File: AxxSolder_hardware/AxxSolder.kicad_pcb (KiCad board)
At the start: 2 copper layers, 39 x 82.5 mm, 143 parts, among them IC1 TLV76733DRVR, IC2 OPA2387DSGT, IC3 LMR54406DBVR, IC4 STM32G431CBT6, IC5 TPD4E1U06DBVR, IC6 STUSB4500QTR, IC7 MAX16171ATA_VY+T, IC8 LTC4440AHMS8E, IC9 INA281A5QDBVRQ1, J1 USB4110-GF-A, J2 691243110009, J3 TSW-102-07-T-S, J4 61300611821, J5 TSW-102-07-T-S, J6 TSW-102-07-T-S, Q1 STL9P3LLH6, Q2 STL10N3LLH5, Q3 2N7002NXAKR, U2 PEC11J-9215F-S0015, U3 BSC014N04LS

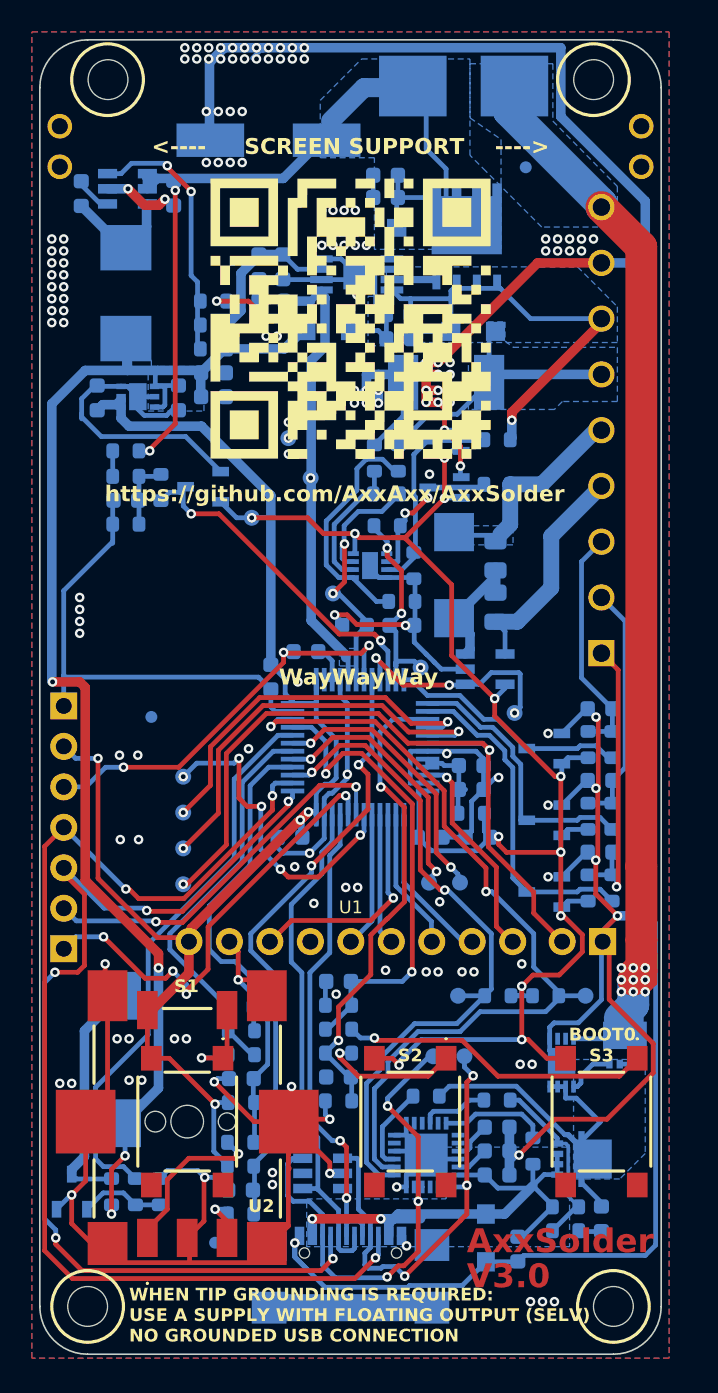
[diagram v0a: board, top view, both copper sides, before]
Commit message: Update hardware files to match correctly with current version
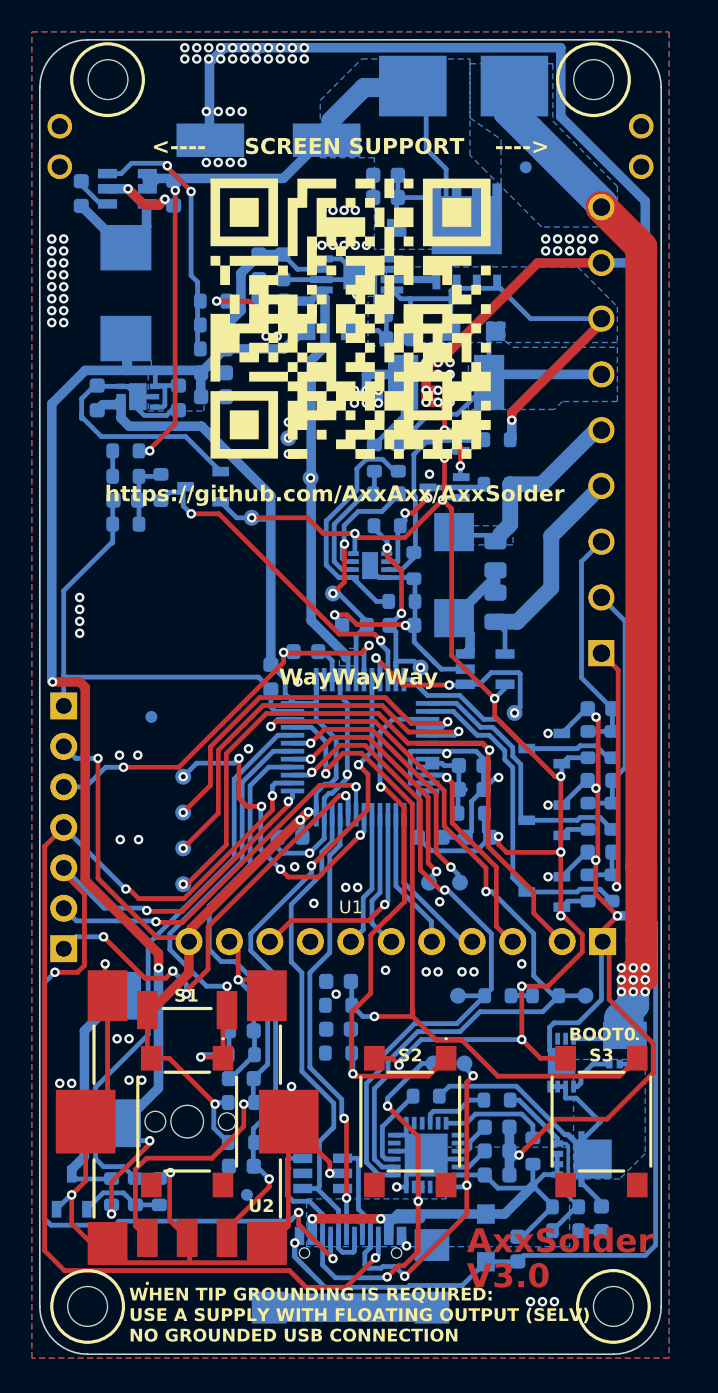
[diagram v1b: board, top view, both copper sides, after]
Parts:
- removed R16, R43, R46, R47, R48: 100, Resistor_SMD:R_0603_1608Metric
- moved FID2 3.61 mm to (174.0, 140.0)
- moved C22 3.00 mm to (179.8, 129.6)
- moved R31 3.00 mm to (179.8, 131.1)
- moved C29 1.50 mm to (173.7, 138.2)
- moved C21 1.50 mm to (173.7, 129.7)
- moved R30 1.50 mm to (173.7, 131.2)
- moved R36 1.49 mm to (173.7, 136.7)
- moved TP7 0.45 mm to (187.7, 131.8)
- moved TP8 0.45 mm to (185.7, 131.8)
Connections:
- J1 pad S1: (no net) -> unconnected-(J1-SHIELD-PadS1)
- S1 pad 1: /S1 -> /SW1
- S2 pad 1: Net-(R43-Pad2) -> /SW2
- S3 pad 1: Net-(R46-Pad2) -> /SW3
- U2 pad A1: Net-(R47-Pad2) -> /ENC_B
- U2 pad C1: Net-(R48-Pad2) -> /ENC_A
- U2 pad E1: /S1 -> /SW1
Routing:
- net Net-(R46-Pad2): track 19.7 -> 0.00 mm, vias 1 -> 0
- net /SW3: track 30.4 -> 47.3 mm
- net GND: track 460.3 -> 447.9 mm, vias 157 -> 149
- net /ENC_B: track 29.0 -> 41.0 mm, vias 0 -> 1
- net Net-(R47-Pad2): track 10.3 -> 0.00 mm, vias 1 -> 0
- net (no net): track 10.2 -> 0.00 mm
- net unconnected-(J1-SHIELD-PadS1): track 0.00 -> 10.2 mm
- net Net-(R43-Pad2): track 9.08 -> 0.00 mm, vias 1 -> 0
- net /SW2: track 30.1 -> 36.6 mm
- net /S1: track 6.25 -> 0.00 mm, vias 1 -> 0
- net /SW1: track 25.3 -> 30.3 mm, vias 0 -> 2
- net /ENC_A: track 38.3 -> 41.5 mm, vias 2 -> 3
- net Net-(R48-Pad2): track 2.95 -> 0.00 mm, vias 1 -> 0
- net +7.5V: track 94.1 -> 95.8 mm
- net /USB_D+: track 32.5 -> 33.4 mm

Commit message: Update hw design with button filters, optimized traces and better silkscreen
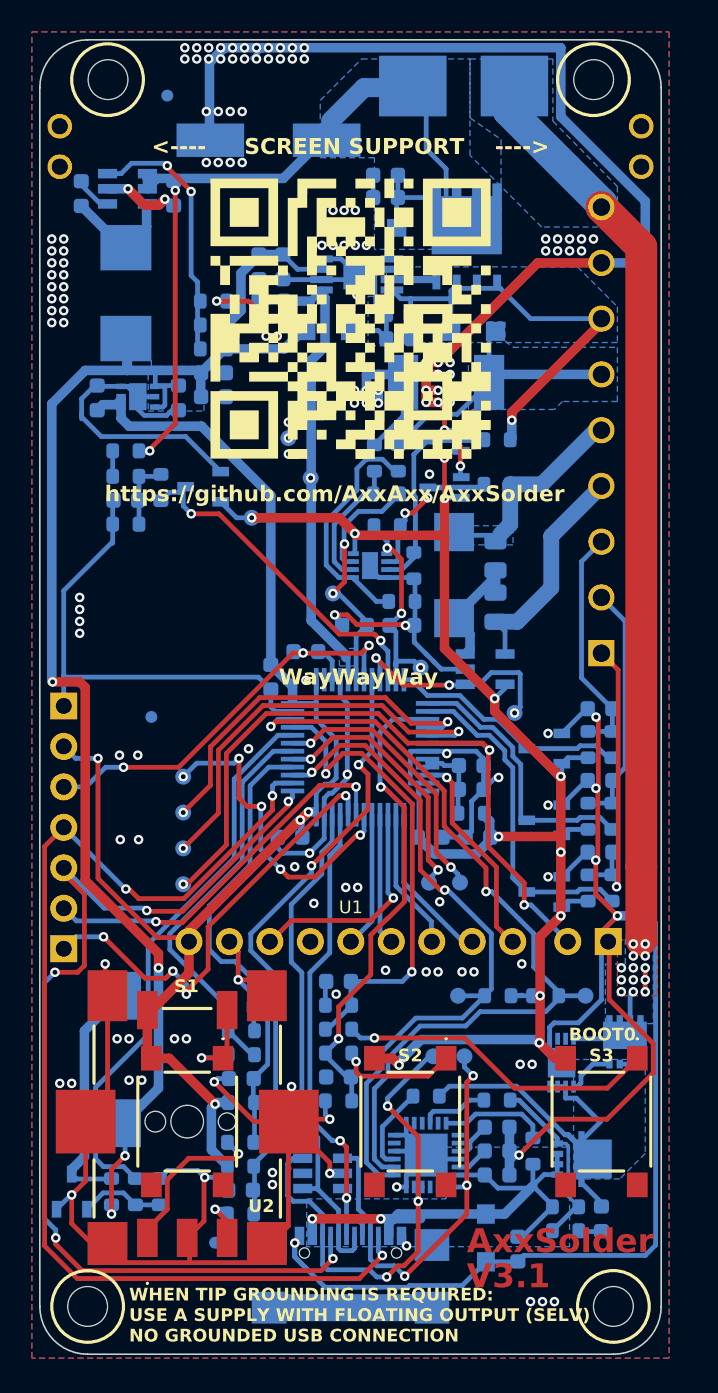
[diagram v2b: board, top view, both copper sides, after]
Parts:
- added R16: 100, Resistor_SMD:R_0603_1608Metric, B.Cu at (173.7, 131.2)
- added R43: 100, Resistor_SMD:R_0603_1608Metric, B.Cu at (179.8, 131.1)
- added R46: 100, Resistor_SMD:R_0603_1608Metric, B.Cu at (179.8, 129.6)
- added R47: 100, Resistor_SMD:R_0603_1608Metric, B.Cu at (173.6, 136.7)
- added R48: 100, Resistor_SMD:R_0603_1608Metric, B.Cu at (173.6, 141.2)
- moved FID3 22.9 mm to (169.0, 71.0)
- moved FID2 3.61 mm to (172.0, 143.0)
- moved C22 3.00 mm to (179.8, 132.6)
- moved R31 3.00 mm to (179.8, 134.1)
- moved C29 1.50 mm to (173.6, 139.7)
- moved C21 1.50 mm to (173.7, 128.2)
- moved R30 1.50 mm to (173.7, 129.7)
- moved R36 1.49 mm to (173.6, 138.2)
- moved TP7 0.45 mm to (187.7, 131.3)
- moved TP8 0.45 mm to (185.7, 131.3)
- moved J3 0.35 mm to (196.7, 124.1)
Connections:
- J1 pad S1: unconnected-(J1-SHIELD-PadS1) -> (no net)
- S1 pad 1: /SW1 -> /S1
- S2 pad 1: /SW2 -> Net-(R43-Pad2)
- S3 pad 1: /SW3 -> Net-(R46-Pad2)
- U2 pad A1: /ENC_B -> Net-(R47-Pad2)
- U2 pad C1: /ENC_A -> Net-(R48-Pad2)
- U2 pad E1: /SW1 -> /S1
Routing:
- net Net-(R46-Pad2): track 0.00 -> 20.5 mm, vias 0 -> 1
- net /SW3: track 47.3 -> 30.4 mm
- net GND: track 447.9 -> 460.3 mm, vias 149 -> 157
- net /ENC_B: track 41.0 -> 29.0 mm, vias 1 -> 0
- net Net-(R47-Pad2): track 0.00 -> 10.3 mm, vias 0 -> 1
- net unconnected-(J1-SHIELD-PadS2): track 0.00 -> 10.2 mm
- net unconnected-(J1-SHIELD-PadS1): track 10.2 -> 0.00 mm
- net Net-(R43-Pad2): track 0.00 -> 7.94 mm, vias 0 -> 1
- net /VDD_IN: track 71.9 -> 64.4 mm, vias 9 -> 13
- net /SW2: track 36.6 -> 30.1 mm
- net /S1: track 0.00 -> 6.25 mm, vias 0 -> 1
- net +3.3V: track 199.4 -> 194.2 mm
- net /SW1: track 30.3 -> 25.3 mm, vias 2 -> 0
- net /ENC_A: track 41.5 -> 38.3 mm, vias 3 -> 2
- net Net-(R48-Pad2): track 0.00 -> 2.95 mm, vias 0 -> 1
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- added copper zone on F.Cu, net /VDD_IN
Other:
- board text added: "2024-06"
- board text added: "CC1-2"
- board text added: "L"
- board text added: "V3.1"
- board text removed: "2024-02"
- board text removed: "V3.0"

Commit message: Updates on schematic and board layout to hw3_1, optimizations and improvement on layout
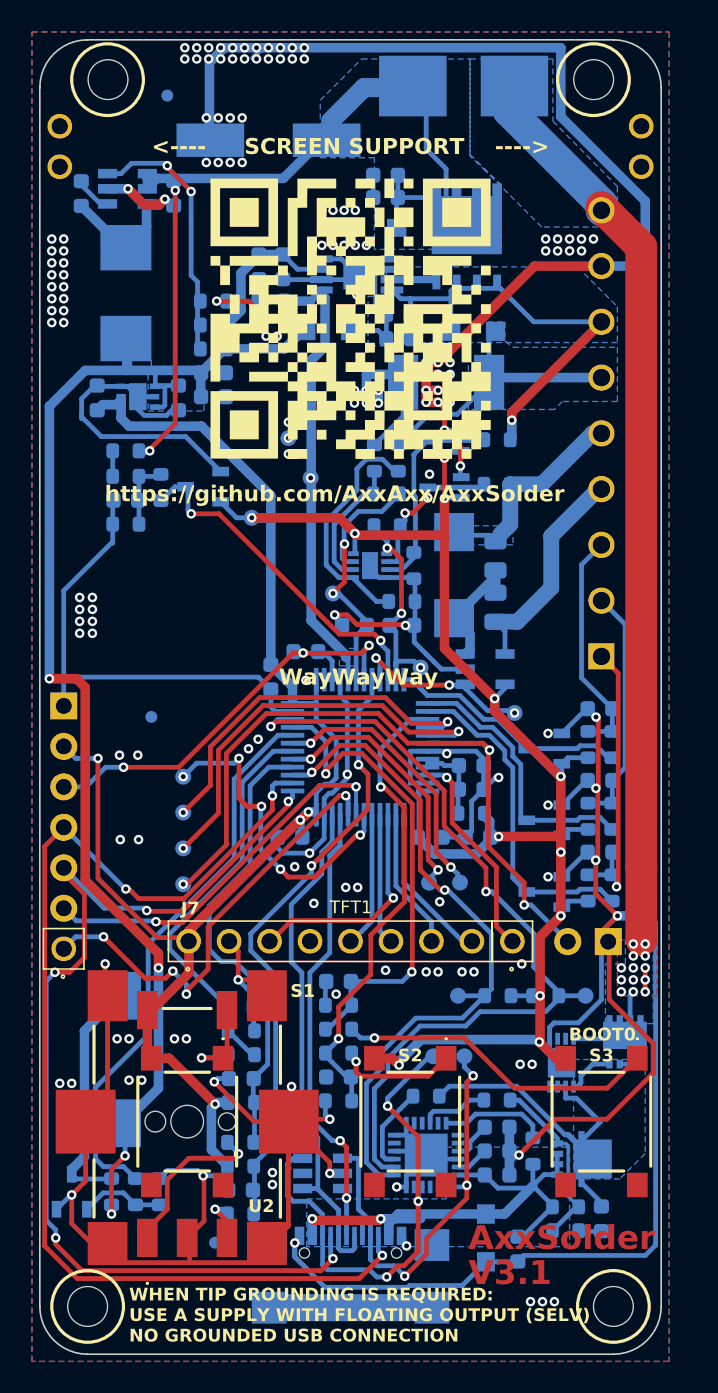
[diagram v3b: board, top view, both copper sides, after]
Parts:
- added J7: TSW-108-07-T-S, footprints:TSW-108-XX-YY-S, F.Cu at (170.3, 124.1)
- added TP18: DIAG_TP, footprints:TSW-101-XX-YY-S, F.Cu at (190.7, 124.1)
- TP13: footprint Connector_PinSocket_2.54mm:PinSocket_1x01_P2.54mm_Vertical -> footprints:TSW-101-XX-YY-S; moved to F.Cu
- moved J2 0.20 mm to (196.2, 106.2)
- renumbered U1 to TFT1
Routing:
- net /I_LEAK: track 14.3 -> 11.9 mm
- net +3.3V: track 194.2 -> 193.4 mm
- net /USART_RX: track 29.0 -> 28.3 mm
- net /SW2: track 30.1 -> 29.5 mm
- net GND: track 460.3 -> 460.5 mm, vias 157 -> 162

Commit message: Update routing
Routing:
- net GND: track 460.5 -> 430.7 mm, vias 162 -> 165
- net /VDD_IN_USBCPD: track 22.7 -> 17.1 mm
- net /USR4: track 46.4 -> 44.4 mm
- net /VDD_IN: track 64.6 -> 66.4 mm
- net +3.3V: track 193.4 -> 195.1 mm
- net /SWDIO: track 64.7 -> 63.9 mm
- net /USR1: track 20.3 -> 19.7 mm
- net Net-(R48-Pad2): track 2.95 -> 3.47 mm
- net /SWCLK: track 70.9 -> 71.0 mm, vias 3 -> 5
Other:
- board text added: "2024-09"
- board text removed: "2024-06"

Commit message: update routing and silkscreen
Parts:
- J2: value 691243110009 -> 691243110008
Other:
- board text added: "2024-06"
- board text removed: "2024-09"
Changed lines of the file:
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@@
         (effects (font (size 0.8 0.8) (thickness 0.15)) (justify mirror))
     )
-    (fp_text value "691243110009" (at -12.25 0.15 90) (layer "B.SilkS") hide
+    (fp_text value "691243110008" (at -12.25 0.15 90) (layer "B.SilkS") hide
         (effects (font (size 0.8 0.8) (thickness 0.15)) (justify mirror))
     )
@@
         (effects (font (size 0.8 0.8) (thickness 0.15)) (justify mirror))
     )
+    (fp_line (start -29.75 -3.5) (end -29.75 3.6)
+      (stroke (width 0.1) (type solid)) (layer "B.SilkS"))
+    (fp_line (start -29.75 3.6) (end 1.75 3.6)
+      (stroke (width 0.1) (type solid)) (layer "B.SilkS"))
+    (fp_line (start 1.75 -3.5) (end -29.75 -3.5)
+      (stroke (width 0.1) (type solid)) (layer "B.SilkS"))
+    (fp_line (start 1.75 3.6) (end 1.75 -3.5)
+      (stroke (width 0.1) (type solid)) (layer "B.SilkS"))
+    (fp_rect (start -28.9 3) (end -27.1 3.6)
+      (stroke (width 0.1) (type default)) (fill none) (layer "B.SilkS"))
+    (fp_rect (start -25.4 3) (end -23.6 3.6)
+      (stroke (width 0.1) (type default)) (fill none) (layer "B.SilkS"))
+    (fp_rect (start -21.9 3) (end -20.1 3.6)
+      (stroke (width 0.1) (type default)) (fill none) (layer "B.SilkS"))
+    (fp_rect (start -18.4 3) (end -16.6 3.6)
+      (stroke (width 0.1) (type default)) (fill none) (layer "B.SilkS"))
+    (fp_rect (start -14.9 3) (end -13.1 3.6)
+      (stroke (width 0.1) (type default)) (fill none) (layer "B.SilkS"))
+    (fp_rect (start -11.4 3) (end -9.6 3.6)
+      (stroke (width 0.1) (type default)) (fill none) (layer "B.SilkS"))
+    (fp_rect (start -7.9 3) (end -6.1 3.6)
+      (stroke (width 0.1) (type default)) (fill none) (layer "B.SilkS"))
+    (fp_rect (start -4.4 3) (end -2.6 3.6)
+      (stroke (width 0.1) (type default)) (fill none) (layer "B.SilkS"))
+    (fp_rect (start -0.9 3) (end 0.9 3.6)
+      (stroke (width 0.1) (type default)) (fill none) (layer "B.SilkS"))
     (fp_line (start -30.75 -4.5) (end -30.75 4.8)
       (stroke (width 0.1) (type solid)) (layer "B.CrtYd"))
@@
     (effects (font (size 0.8 0.8) (thickness 0.15) bold) (justify left bottom))
   )
-  (gr_text "2024-09" (at 187.3 148.8) (layer "B.Mask")
+  (gr_text "2024-06" (at 187.3 148.8) (layer "B.Mask")
     (effects (font (size 1 1) (thickness 0.2) bold) (justify right mirror))
   )
@@
       (effects (font (size 1 1) (thickness 0.15)))
     )
+    (format (prefix "") (suffix "") (units 3) (units_format 1) (precision 4))
+    (style (thickness 0.15) (arrow_length 1.27) (text_position_mode 0) (extension_height 0.58642) (extension_offset 0.5) keep_text_aligned)
+  )
+  (dimension (type aligned) (layer "User.4")
+    (pts (xy 164 67.5) (xy 164 150))
+    (height 6.499999)
+    (gr_text "82,5000 mm" (at 156.350001 108.75 90) (layer "User.4")
+      (effects (font (size 1 1) (thickness 0.15)))
+    )

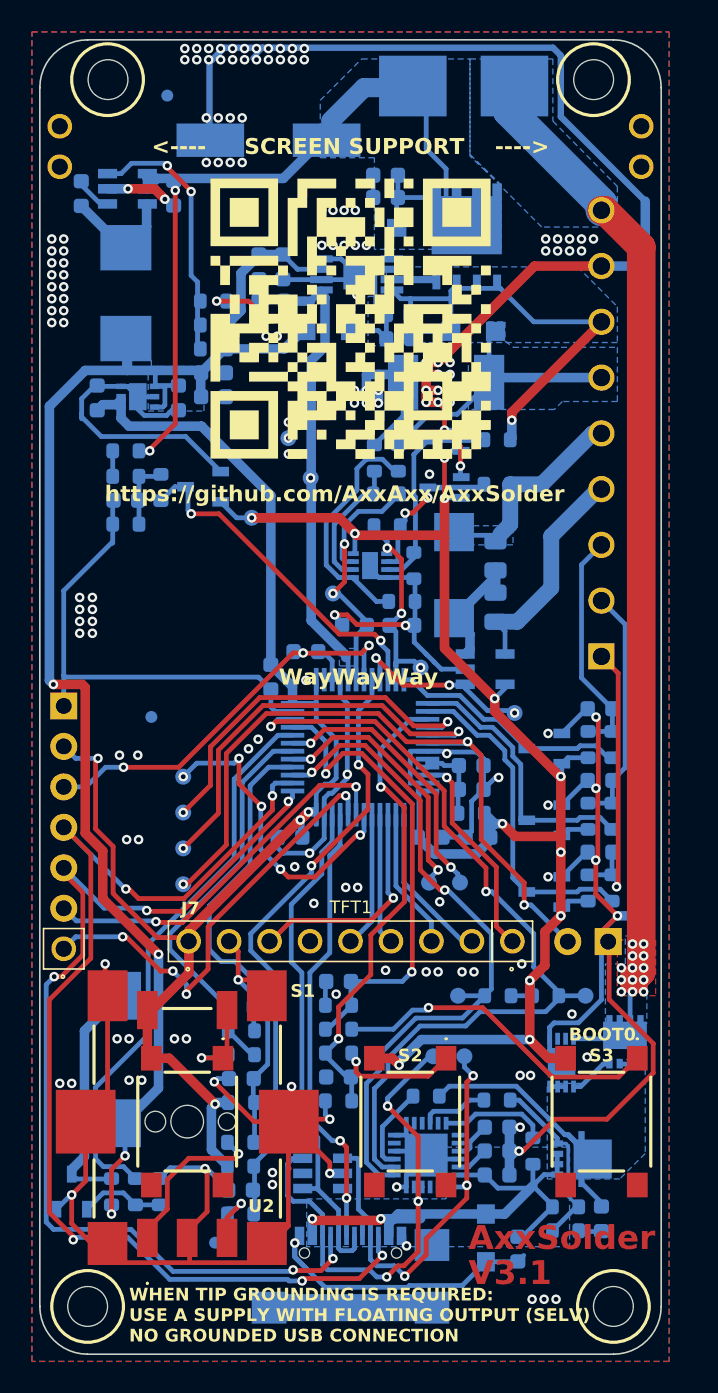
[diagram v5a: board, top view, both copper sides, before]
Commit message: Minor update on trace layout
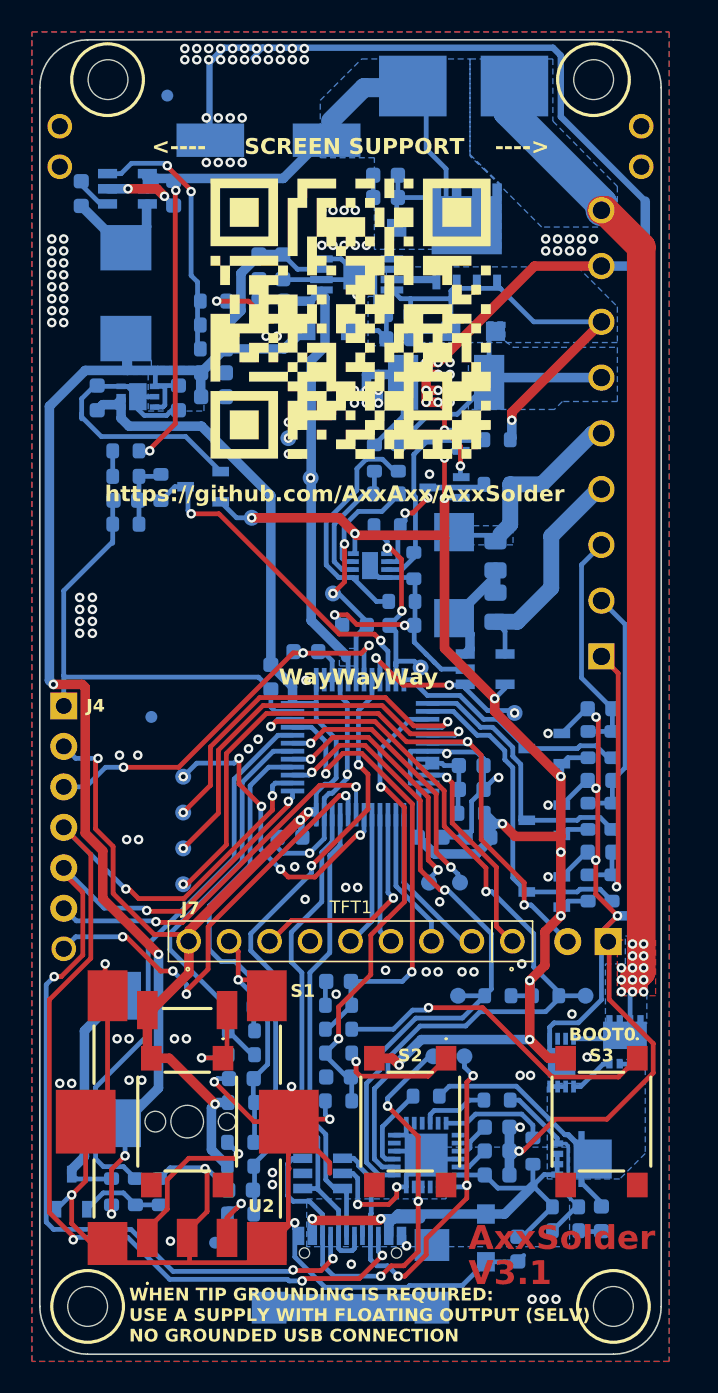
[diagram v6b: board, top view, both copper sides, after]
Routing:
- net GND: track 430.7 -> 435.5 mm, vias 165 -> 167
- net /USB_D-: track 31.0 -> 30.3 mm, vias 2 -> 0
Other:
- board text added: "2024-09"
- board text removed: "2024-06"
